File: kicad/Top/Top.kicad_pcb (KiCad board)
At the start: 4 copper layers, 143.5 x 101.6 mm, 295 parts, among them J1 ED120/2DS, J10 Header 2x3, J13 Header 2x5, J14 PACK CONNECT, J15 CELL CONNECT, J2 ED120/2DS, J3 ED120/2DS, J4 USBC_Receptacle_SMD_RA, J5 ED120/4DS, J6 M20-9990246, J8 0022053041, J9 N2510-6002-RB, Q1 CSD17581Q3A, Q2 CSD17581Q3A, Q3 CSD17581Q3A, Q4 CSD17581Q3A, Q5 CSD17575Q3, Q6 SI4477DY-T1-GE3, Q7 SI4477DY-T1-GE3, Q8 PMBF170,235, Q9 PMBF170,235, U1 BQ25790YBG, U2 TLV76033DBZR, U3 MCP1804 SOT-23-5, U4 UPD301C QFN-40, U5 EFC8811R-TF, U6 BQ2980RUG

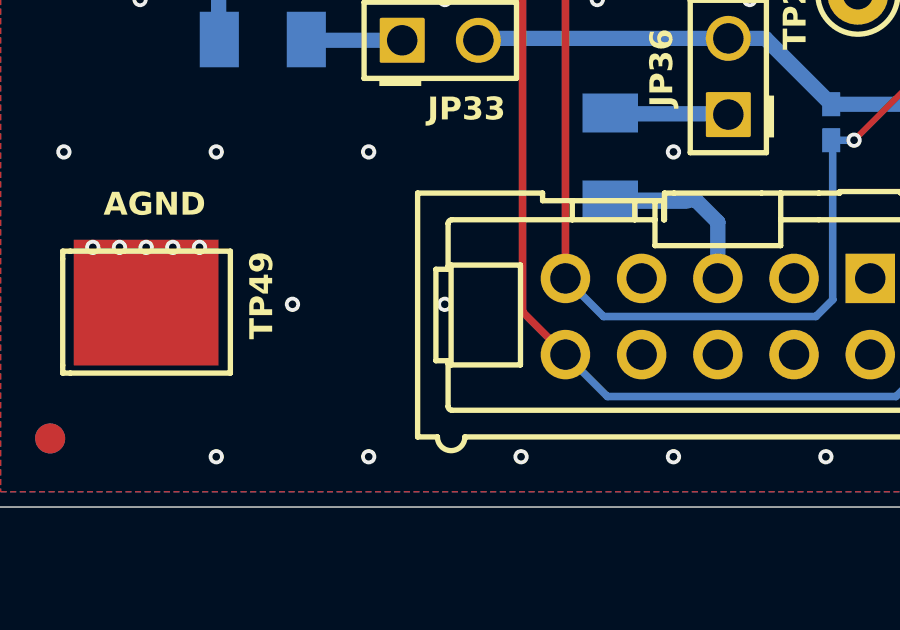
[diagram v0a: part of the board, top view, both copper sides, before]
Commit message: Properly synced pcb to schematic
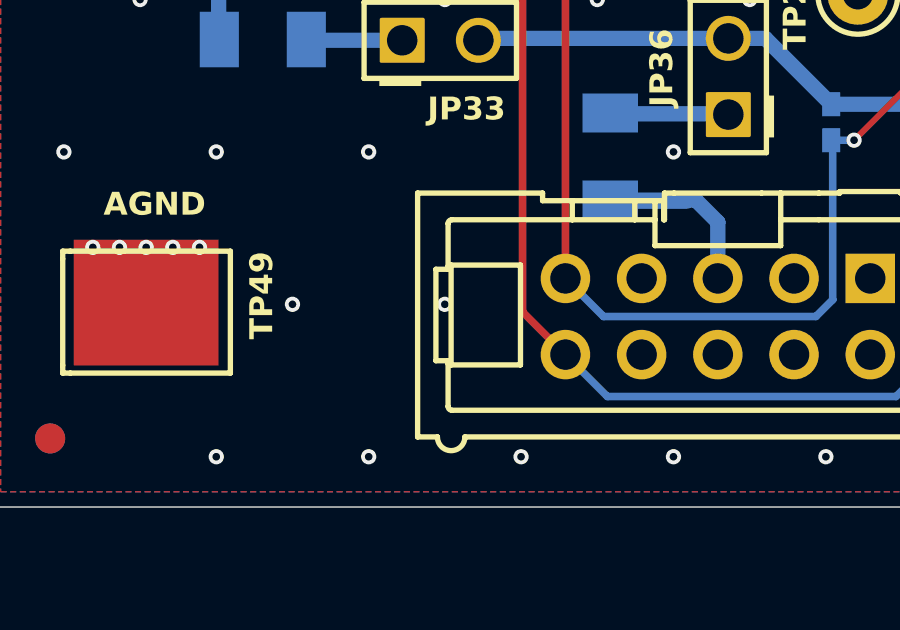
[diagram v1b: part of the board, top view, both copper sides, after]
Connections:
- net /CE renamed /CE
- net /INT renamed /INT
- net /PG renamed /PG
- net /QON renamed /QON
- net 1.5A_IND renamed /Designator/Designator/1.5A_IND
- net 3.0A_IND renamed /Designator/Designator/3.0A_IND
- net BAT_PRO renamed /Designator/BAT_PRO
- net BAT_Physical renamed /Designator/BAT_Physical
- net BTST1 renamed /Designator/U_Charger_Circuit/BTST1
- net BTST2 renamed /Designator/U_Charger_Circuit/BTST2
- net CAP_MISMATCH renamed /Designator/Designator/CAP_MISMATCH
- net CC1 renamed /Designator/Designator/CC1
- net CC1_R renamed /Designator/Designator/CC1_R
- net CC2 renamed /Designator/Designator/CC2
- net CC2_R renamed /Designator/Designator/CC2_R
- net CS renamed /Designator/CS
- net CTR renamed /Designator/CTR
- net D+_1 renamed /Designator/U_Charger_Circuit/D+_1
- net D-_1 renamed /Designator/U_Charger_Circuit/D-_1
- net DAC_I renamed /Designator/Designator/DAC_I
- net EN_SNK renamed /Designator/Designator/EN_SNK
- net FAULT_IN_N renamed /Designator/Designator/FAULT_IN_N
- net IBAT renamed /Designator/U_Charger_Circuit/IBAT
- net NetC12_1 renamed Net-(C12-Pad1)
- net NetC18_2 renamed Net-(C18-Pad2)
- net NetC2_1 renamed Net-(C2-Pad1)
- net NetC2_2 renamed Net-(C2-Pad2)
- net NetC39_2 renamed Net-(C39-Pad2)
- net NetC40_1 renamed Net-(C40-Pad1)
- net NetC42_2 renamed Net-(C42-Pad2)
- net NetC5_1 renamed Net-(C5-Pad1)
- net NetC5_2 renamed Net-(C5-Pad2)
- net NetC6_1 renamed Net-(C6-Pad1)
- net NetD10_1 renamed Net-(D10-Pad1)
- net NetD11_1 renamed Net-(D11-Pad1)
- net NetD13_1 renamed Net-(D13-Pad1)
- net NetD13_2 renamed Net-(D13-Pad2)
- net NetD14_1 renamed Net-(D14-Pad1)
- net NetD14_2 renamed Net-(D14-Pad2)
- net NetD15_1 renamed Net-(D15-Pad1)
- net NetD17_1 renamed Net-(D17-Pad1)
- net NetD18_1 renamed Net-(D18-Pad1)
- net NetJ10_1 renamed I2C_SLAVE_IRQ
- net NetJ10_2 renamed DEBUG_TRACE_TX
- net NetJ10_3 renamed I2C_SLAVE_SDA
- net NetJ10_4 renamed DEBUG_TRACE_RX
- net NetJ10_5 renamed I2C_SLAVE_SCL
- net NetJ13_2 renamed TRGT_SWDIO
- net NetJ13_4 renamed TRGT_SWCLK
- net NetJ3_1 renamed Net-(J3-Pad1)
- net NetJ8_4 renamed Net-(J8-Pad4)
- net NetJ9_5 renamed Net-(J9-Pad5)
- net NetJP14_2 renamed Net-(JP14-Pad2)
- net NetJP15_2 renamed Net-(JP15-Pad2)
- net NetJP16_2 renamed Net-(JP16-Pad2)
- net NetJP24_2 renamed Net-(JP24-Pad2)
- net NetJP25_2 renamed Net-(JP25-Pad2)
- net NetJP32_2 renamed Net-(JP32-Pad2)
- net NetJP33_1 renamed Net-(JP33-Pad1)
- net NetJP36_1 renamed Net-(JP36-Pad1)
- net NetJP5_1 renamed Net-(JP5-Pad1)
- net NetQ6_4 renamed Net-(Q6-Pad4)
- net NetQ8_3 renamed Net-(Q8-Pad3)
- net NetQ9_3 renamed Net-(Q9-Pad3)
- net NetR38_1 renamed Net-(R38-Pad1)
- net NetR47_2 renamed Net-(R47-Pad2)
- net NetR56_1 renamed PDO_SEL
- net NetR59_1 renamed Net-(R59-Pad1)
- net NetR60_1 renamed Net-(R60-Pad1)
- net NetR64_1 renamed Net-(R64-Pad1)
- net ORIENTATION renamed /Designator/Designator/ORIENTATION
- net PACK renamed /Designator/PACK
- net PMID renamed /Designator/U_Charger_Circuit/PMID
- net SDRV renamed /Designator/U_Charger_Circuit/SDRV
- net SPI_MOSI renamed /Designator/Designator/SPI_MOSI
- net SPI_MOSI_SI renamed /Designator/Designator/SPI_MOSI_SI
- net SW1 renamed /Designator/U_Charger_Circuit/SW1
- net SW2 renamed /Designator/U_Charger_Circuit/SW2
- net VBUS_DIS renamed /Designator/Designator/VBUS_DIS
- net VBUS_F renamed /Designator/Designator/VBUS_F
- net VDD renamed /Designator/VDD
- C1 pad 1: VBUS_USB_OUT -> VIN1
- C33 pad 2: NetC33_2 -> unconnected-(C33-Pad2)
- D16 pad 3: NetC33_2 -> unconnected-(C33-Pad2)
- J1 pad 2: VBUS_USB_OUT -> VIN1
- J13 pad 6: (no net) -> unconnected-(J13-Pad6)
- J13 pad 7: (no net) -> unconnected-(J13-Pad7)
- J13 pad 8: (no net) -> unconnected-(J13-Pad8)
- J14 pad 2: BAT_Protection -> /Designator/BAT_Protection
- J4 pad A10: (no net) -> unconnected-(J4-PadA10)
- J4 pad A11: (no net) -> unconnected-(J4-PadA11)
- J4 pad A2: (no net) -> unconnected-(J4-PadA2)
- J4 pad A3: (no net) -> unconnected-(J4-PadA3)
- J4 pad A8: (no net) -> unconnected-(J4-PadA8)
- J4 pad B10: (no net) -> unconnected-(J4-PadB10)
- J4 pad B11: (no net) -> unconnected-(J4-PadB11)
- J4 pad B2: (no net) -> unconnected-(J4-PadB2)
- J4 pad B3: (no net) -> unconnected-(J4-PadB3)
- J4 pad B8: (no net) -> unconnected-(J4-PadB8)
- J5 pad 4: BAT_Protection -> VBAT
- J9 pad 1: (no net) -> unconnected-(J9-Pad1)
- J9 pad 2: (no net) -> unconnected-(J9-Pad2)
- J9 pad 3: (no net) -> unconnected-(J9-Pad3)
- J9 pad 4: (no net) -> unconnected-(J9-Pad4)
- J9 pad 7: (no net) -> unconnected-(J9-Pad7)
- J9 pad 8: (no net) -> unconnected-(J9-Pad8)
- R13 pad 1: BAT_Protection -> VBAT
- R2 pad 1: VBUS_USB_OUT -> VIN1
- R28 pad 1: NetR28_1 -> unconnected-(R28-Pad1)
- R33 pad 1: NetC33_2 -> unconnected-(C33-Pad2)
- R48 pad 2: NetC33_2 -> unconnected-(C33-Pad2)
- R60 pad 2: BAT_Protection -> /Designator/BAT_Protection
- R63 pad 2: BAT_Protection -> /Designator/BAT_Protection
- TP1 pad 1: VBUS_USB_OUT -> VIN1
- TP18 pad 1: BAT_Protection -> VBAT
- U3 pad 3: (no net) -> unconnected-(U3-Pad3)
- U3 pad 4: NetR28_1 -> unconnected-(R28-Pad1)
- U4 pad 1: (no net) -> unconnected-(U4-Pad1)
- U4 pad 13: (no net) -> unconnected-(U4-Pad13)
- U4 pad 22: (no net) -> unconnected-(U4-Pad22)
- U4 pad 23: (no net) -> unconnected-(U4-Pad23)
- U4 pad 24: (no net) -> unconnected-(U4-Pad24)
- U4 pad 27: (no net) -> unconnected-(U4-Pad27)
- U4 pad 29: (no net) -> unconnected-(U4-Pad29)
- U4 pad 3: (no net) -> unconnected-(U4-Pad3)
- U4 pad 9: NetC33_2 -> unconnected-(C33-Pad2)
- U5 pad 1: BAT_Protection -> /Designator/BAT_Protection
- U5 pad 3: BAT_Protection -> /Designator/BAT_Protection
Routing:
- net ACDRV2: track 122.8 -> 0.00 mm, vias 2 -> 0
- net ACDRV1: track 112.3 -> 235.1 mm, vias 0 -> 2
- net BAT_Protection: track 18.9 -> 0.00 mm, vias 15 -> 0
- net unconnected-(C33-Pad2): track 0.00 -> 16.3 mm, vias 0 -> 2
- net NetC33_2: track 16.3 -> 0.00 mm, vias 2 -> 0
- net PGND: track 97.3 -> 110.6 mm, vias 281 -> 282
- net VIN1: track 0.00 -> 12.1 mm
- net VBUS_USB_OUT: track 12.1 -> 0.00 mm
- net VBAT: track 0.00 -> 12.1 mm
- net AGND: track 33.0 -> 22.0 mm
- net /Designator/BAT_Protection: track 0.00 -> 6.79 mm, vias 0 -> 15
- net unconnected-(R28-Pad1): track 0.00 -> 4.38 mm
- net NetR28_1: track 4.38 -> 0.00 mm
- net (no net): track 17.0 -> 14.8 mm, vias 78 -> 77
- added copper zone on F.Cu, net /Designator/BAT_Protection
- removed copper zone on F.Cu, net BAT_Protection

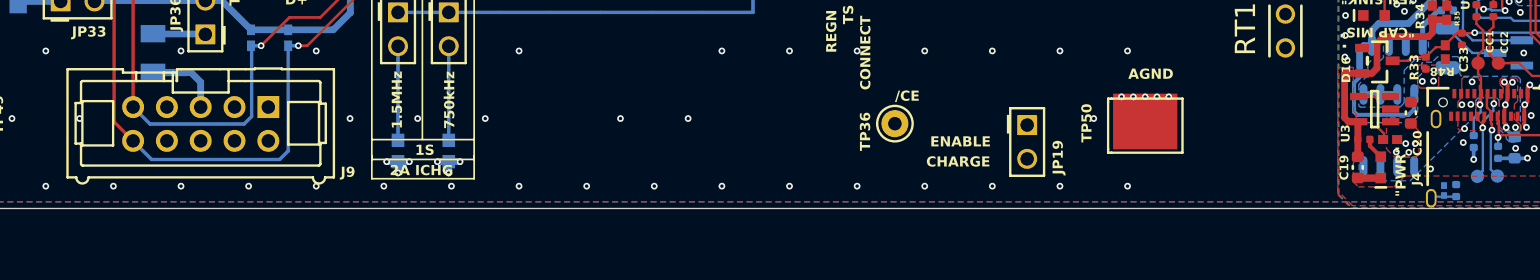
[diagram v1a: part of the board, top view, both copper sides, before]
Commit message: Removed earth net
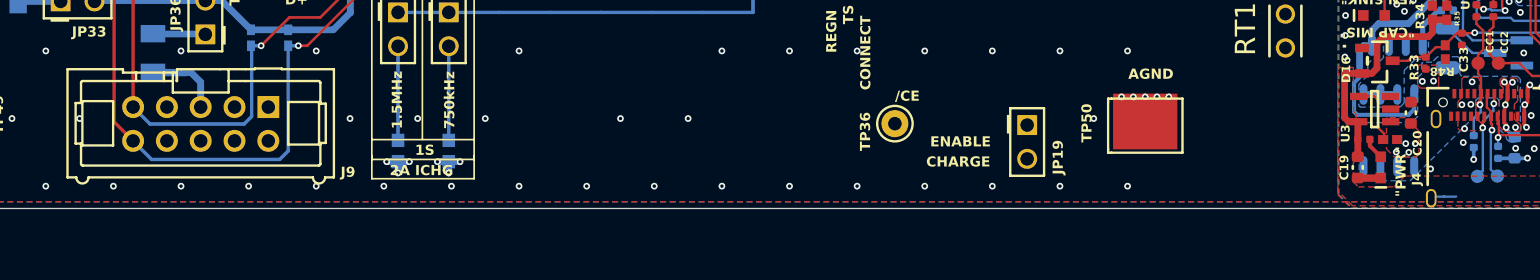
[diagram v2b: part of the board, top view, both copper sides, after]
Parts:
- removed C44: CAP1337, AltiumImports:_ALTIUM_WORK_00001_MCHP-CDB_Library_Database_.._Footprints_CAP_C_0402.PcbLib_CAP_C_0402
- removed R36: CMP-2002-07613-1, AltiumImports:RESC1005X40X25LL05T10
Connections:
- J4 pad 25: EARTH_P1 -> PGND
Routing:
- net PGND: track 110.6 -> 112.5 mm
- net EARTH_P1: track 1.93 -> 0.00 mm

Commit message: Renamed sheets
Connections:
- net /Designator/BAT_PRO renamed /Protection/BAT_PRO
- net /Designator/BAT_Physical renamed /Protection/BAT_Physical
- net /Designator/BAT_Protection renamed /Protection/BAT_Protection
- net /Designator/CS renamed /Protection/CS
- net /Designator/CTR renamed /Protection/CTR
- net /Designator/Designator/1.5A_IND renamed /USB-PD/USB-PD_Circuit/1.5A_IND
- net /Designator/Designator/3.0A_IND renamed /USB-PD/USB-PD_Circuit/3.0A_IND
- net /Designator/Designator/CAP_MISMATCH renamed /USB-PD/USB-PD_Circuit/CAP_MISMATCH
- net /Designator/Designator/CC1 renamed /USB-PD/USB-PD_Circuit/CC1
- net /Designator/Designator/CC1_R renamed /USB-PD/USB-PD_Circuit/CC1_R
- net /Designator/Designator/CC2 renamed /USB-PD/USB-PD_Circuit/CC2
- net /Designator/Designator/CC2_R renamed /USB-PD/USB-PD_Circuit/CC2_R
- net /Designator/Designator/DAC_I renamed /USB-PD/USB-PD_Circuit/DAC_I
- net /Designator/Designator/EN_SNK renamed /USB-PD/USB-PD_Circuit/EN_SNK
- net /Designator/Designator/FAULT_IN_N renamed /USB-PD/USB-PD_Circuit/FAULT_IN_N
- net /Designator/Designator/ORIENTATION renamed /USB-PD/USB-PD_Circuit/ORIENTATION
- net /Designator/Designator/SPI_MOSI renamed /USB-PD/USB-PD_Circuit/SPI_MOSI
- net /Designator/Designator/SPI_MOSI_SI renamed /USB-PD/USB-PD_Circuit/SPI_MOSI_SI
- net /Designator/Designator/VBUS_DIS renamed /USB-PD/USB-PD_Circuit/VBUS_DIS
- net /Designator/Designator/VBUS_F renamed /USB-PD/USB-PD_Circuit/VBUS_F
- net /Designator/PACK renamed /Protection/PACK
- net /Designator/U_Charger_Circuit/BTST1 renamed /Charger/Charger_Circuit/BTST1
- net /Designator/U_Charger_Circuit/BTST2 renamed /Charger/Charger_Circuit/BTST2
- net /Designator/U_Charger_Circuit/D+_1 renamed /Charger/Charger_Circuit/D+_1
- net /Designator/U_Charger_Circuit/D-_1 renamed /Charger/Charger_Circuit/D-_1
- net /Designator/U_Charger_Circuit/IBAT renamed /Charger/Charger_Circuit/IBAT
- net /Designator/U_Charger_Circuit/PMID renamed /Charger/Charger_Circuit/PMID
- net /Designator/U_Charger_Circuit/SDRV renamed /Charger/Charger_Circuit/SDRV
- net /Designator/U_Charger_Circuit/SW1 renamed /Charger/Charger_Circuit/SW1
- net /Designator/U_Charger_Circuit/SW2 renamed /Charger/Charger_Circuit/SW2
- net /Designator/VDD renamed /Protection/VDD
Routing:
- net ACDRV2: track 0.00 -> 122.8 mm, vias 0 -> 2
- net ACDRV1: track 235.1 -> 112.3 mm, vias 2 -> 0
- net AGND: track 22.0 -> 33.0 mm, vias 40 -> 41
- net PGND: track 112.5 -> 101.5 mm, vias 282 -> 281

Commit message: Cleared pcb
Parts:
- removed C1, C4: CMP-0008217-2, AltiumImports:0805L
- removed C10, C21, C22, C23, C27, C28, C29, C30, C31, C7, C8, C9: C2012X5R1E106K125AB, AltiumImports:0805_HV
- removed C11, C14, C15, C24, C26: C1005X7R1H104K050BE, AltiumImports:0402L
- removed C12, C6: GRM1885C1H222JA01D, AltiumImports:0603
- removed C13, C3: GRM155R71E473KA88D, AltiumImports:0402
- removed C16, C17: C0402C103J5RACTU, AltiumImports:0402
- removed C18, C46: Capacitor NP, AltiumImports:_ALTIUM_WORK_00001_MCHP-CDB_Library_Database_MCHP-CDB.DbLib_Capacitor_CAP_C_0603
- removed C19, C20: Capacitor NP, AltiumImports:_ALTIUM_WORK_00001_MCHP-CDB_Library_Database_.._Footprints_CAP_C_0603.PcbLib_CAP_C_0603
- removed C2, C39, C5: GRM1555C1H102FA01D, AltiumImports:0402
- removed C25, C32, C47, C48: Capacitor NP, AltiumImports:_ALTIUM_WORK_00001_MCHP-CDB_Library_Database_MCHP-CDB.DbLib_Capacitor_CAP_C_0402
- removed C33, C45, C53: CAP1337, AltiumImports:_ALTIUM_WORK_00001_MCHP-CDB_Library_Database_.._Footprints_CAP_C_0402.PcbLib_CAP_C_0402
- removed C34: GRM188R61C475KAAJD, AltiumImports:0603L
- removed C35, C42, C43: GRM155R61E104KA87D, AltiumImports:0402L
- removed C36, C37, C38: GRT188R61E106ME13D, AltiumImports:0603L
- removed C40, C41: GRM1555C1H102JA01D, AltiumImports:0402L
- removed C49, C51, C52: CAP1337, AltiumImports:CAP_C_0402
- removed C50: Capacitor NP, AltiumImports:CAP_C_0603
- removed C54, C55, C56: GRM188R71H104KA93D, AltiumImports:0603L
- removed D1, D10, D4: CMP-0028378-3, AltiumImports:SOD-523
- removed D11, D12: BAT54HT1G, AltiumImports:SOD-323
- removed D13, D14: LTST-C190GKT, AltiumImports:LED_LTST-C190
- removed D15, D17: LED_green, AltiumImports:_ALTIUM_WORK_00001_MCHP-CDB_Library_Database_.._Footprints_LED_0603_Green.PcbLib_LED_0603_GREEN
- removed D16: Diode Dual AK, AltiumImports:SOT-23-3
- removed D18: LED_orange, AltiumImports:_ALTIUM_WORK_00001_MCHP-CDB_Library_Database_.._Footprints_LED_0603_Orange.PcbLib_LED_0603_Orange
- removed D2, D5, D9: BZT52C12T-7, AltiumImports:SOD-523
- removed D3, D6, D7, D8: B130LAW-7-F, AltiumImports:SOD-123
- removed FB1: Ferrite Bead, AltiumImports:IND_C_0603
- removed FID1, FID2, FID3, FID4, FID5, FID6: CMP-0077181-1, AltiumImports:Fiducial10-20
- removed H1, H2, H3, H4: SJ-5303 (CLEAR), AltiumImports:Bumpon_SJ5003Transparent
- removed J1, J2, J3: ED120/2DS, AltiumImports:On-Shore_ED120_2DS
- removed J10: Header 2x3, AltiumImports:_ALTIUM_WORK_00001_MCHP-CDB_Library_Database_MCHP-CDB.DbLib_Connector_HDR_M_2.54_2x3
- removed J13: Header 2x5, AltiumImports:_ALTIUM_WORK_00001_MCHP-CDB_Library_Database_MCHP-CDB.DbLib_Connector_HDR_M_1.27_2x5_TH_V_FCI_20021111-00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
- removed J14: PACK CONNECT, AltiumImports:TERM_BLK_ED555-2DS
- removed J15: CELL CONNECT, AltiumImports:TERM_BLK_ED555-2DS
- removed J4: USBC_Receptacle_SMD_RA, AltiumImports:CON_USB3.1-C_RCPT_SMD_RA_ACP_12401610E4#2A
- removed J5: ED120/4DS, AltiumImports:On-Shore_ED120_4DS
- removed J6: M20-9990246, AltiumImports:FP-M20-9990246-MFG
- removed J8: 0022053041, AltiumImports:CONN_22-05-3041
- removed J9: N2510-6002-RB, AltiumImports:CONN_2510-6002
- removed JP1, JP11, JP2: PEC03SAAN, AltiumImports:CONN_PEC03SAAN
- removed JP10, JP19, JP32, JP33, JP34, JP35, JP36, JP6: Header_2x1, AltiumImports:CONN_PEC02SAAN
- removed JP12, JP13, JP14, JP15, JP16, JP23, JP24, JP25, JP9: CMP-0002337-1, AltiumImports:CONN_PEC02SAAN
- removed JP3, JP4, JP5: HTSW-102-07-G-S, AltiumImports:Samtec_HTSW-102-07-G-S
- removed L1: MPIM252010F1R0M-LF, AltiumImports:MPIM252010F
- removed L2: SPM6530T-2R2M, AltiumImports:SPM6530
- removed LOGO5: CAUTION HOT SURFACE, AltiumImports:IEC_HotSurface_Small
- removed NT1: CMP-0078142-3, AltiumImports:Net-Tie_20milWide_60milLong
- removed Q1, Q2, Q3, Q4: CSD17581Q3A, AltiumImports:DNH0008A
- removed Q5: CSD17575Q3, AltiumImports:DQG0008A
- removed Q6, Q7: SI4477DY-T1-GE3, AltiumImports:_ALTIUM_WORK_00001_MCHP-CDB_Library_Database_.._Footprints_SOIC-8.PcbLib_SOIC-8
- removed Q8, Q9: PMBF170,235, AltiumImports:NXP-SOT23_M
- removed R1, R14, R38, R5: 5106, AltiumImports:5106
- removed R10, R8: CRCW06032R00JNEA, AltiumImports:0603
- removed R11: Resistor, AltiumImports:RES_C_1206
- removed R12, R13, R2, R6: WSL2010R0100FEA18, AltiumImports:2010
- removed R15, R3, R7: RC0402FR-07100KL, AltiumImports:0402
- removed R16: CMP-0025697-4, AltiumImports:0603L
- removed R17, R18: RC0603FR-07100RL, AltiumImports:0603
- removed R19: CMP-0026464-2, AltiumImports:0402
- removed R20, R42, R43, R44, R45: CRCW040210K0FKED, AltiumImports:0402
- removed R21: 47k, AltiumImports:FP-CRCW0603-e3-IPC_B
- removed R22: CRCW0603255KFKEA, AltiumImports:0603
- removed R23, R24, R27, R33, R50, R52, R56: Resistor, AltiumImports:_ALTIUM_WORK_00001_MCHP-CDB_Library_Database_MCHP-CDB.DbLib_Resistor_RES_C_0402
- removed R25: RC0603FR-07100KL, AltiumImports:0603
- removed R26: CMP-0026284-2, AltiumImports:0402
- removed R28, R34, R35, R48, R54, R55: CRGP0402F10K, AltiumImports:FP-CRGP0402-IPC_A
- removed R29: RC0603FR-073KL, AltiumImports:0603
- removed R30: RC0603FR-074K7L, AltiumImports:0603
- removed R31, R49: Resistor, AltiumImports:_ALTIUM_WORK_00001_MCHP-CDB_Library_Database_MCHP-CDB-Offline.DbLib_Resistor_RES_C_0402
- removed R32, R47, R51, R53, R57, R58: Resistor, AltiumImports:_ALTIUM_WORK_00001_MCHP-CDB_Library_Database_.._Footprints_RES_C_0402.PcbLib_RES_C_0402
- removed R37, R39, R46: ERJ-8ENF10R0V, AltiumImports:1206
- removed R4, R9: CRCW0603294RFKEA, AltiumImports:0603
- removed R40, R41: CRCW04022K21FKED, AltiumImports:0402
- removed R59, R60: CRCW04025M10JNED, AltiumImports:0402L
- removed R61: CRCW0402330RJNED, AltiumImports:0402L
- removed R62: CRCW040220R0FKED, AltiumImports:0402L
- removed R63: CRCW04022K00FKED, AltiumImports:0402L
- removed R64: CRCW0402100RFKED, AltiumImports:0402L
- removed R65: R_SEN, AltiumImports:1206
- removed RT1: 103AT-2, AltiumImports:SEMI-103AT-2_V
- removed S1: CMP-0002170-2, AltiumImports:KSR
- removed SH-JP1: ACDRV1 to _acdrv1, AltiumImports:FP-SNT-100-BK-G-MFG
- removed SH-JP10, SH-JP11, SH-JP12, SH-JP14, SH-JP16, SH-JP19, SH-JP32, SH-JP34, SH-JP35, SH-JP36, SH-JP37, SH-JP6, SH-JP9: Installed, AltiumImports:FP-SNT-100-BK-G-MFG
- removed SH-JP13, SH-JP15, SH-JP23, SH-JP24, SH-JP25, SH-JP3, SH-JP33, SH-JP4, SH-JP5: Not Installed, AltiumImports:FP-SNT-100-BK-G-MFG
- removed SH-JP2: ACDRV2 to _acdrv2, AltiumImports:FP-SNT-100-BK-G-MFG
- removed TP1, TP10, TP11, TP12, TP15, TP16, TP17, TP18, TP19, TP2, TP20, TP28, TP29, TP3, TP30, TP31, TP32, TP33, TP34, TP35, TP36, TP37, TP38, TP39, TP4, TP40, TP41, TP42, TP43, TP44, TP5, TP6, TP7, TP8, TP9: CMP-0055139-1, AltiumImports:Keystone5002
- removed TP13, TP14, TP52, TP53, TP54, TP55, TP56, TP57, TP58, TP59: Test Point No BOM, AltiumImports:_ALTIUM_WORK_00001_MCHP-CDB_Library_Database_.._Footprints_TP_1mm_SMD.PcbLib_TP_1mm_SMD
- removed TP21, TP22, TP23, TP24: CMP-0055137-1, AltiumImports:Keystone5000
- removed TP25, TP26: CMP-0055140-1, AltiumImports:Keystone5003
- removed TP27: CMP-0055141-1, AltiumImports:Keystone5004
- removed TP45, TP46, TP47, TP48, TP49, TP50, TP51: CMP-0055153-1, AltiumImports:Testpoint_Keystone_Compact
- removed TP60: G_CHG, AltiumImports:TESTPOINT
- removed TP61: G_DSG, AltiumImports:TESTPOINT
- removed TP62: CTR, AltiumImports:Keystone5012
- removed U1: BQ25790YBG, AltiumImports:PREYBG0056
- removed U2: TLV76033DBZR, AltiumImports:DBZ0003A_N
- removed U3: MCP1804 SOT-23-5, AltiumImports:_ALTIUM_WORK_00001_MCHP-CDB_Library_Database_MCHP-CDB.DbLib_MCHP-Analog_SOT-23-5
- removed U4: UPD301C QFN-40, AltiumImports:_ALTIUM_WORK_00001_MCHP-CDB_Library_Database_MCHP-CDB.DbLib_MCHP-Interface_QFN-40_6X6_m5_4m6epad
- removed U5: EFC8811R-TF, AltiumImports:CSP6_568AL
- removed U6: BQ2980RUG, AltiumImports:RUG0008A
- moved ZZ1 26.5 mm to (59.6, 16.6)
- moved ZZ2 26.5 mm to (59.6, 22.9)
- moved ZZ3 26.5 mm to (59.6, 29.3)
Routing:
- net REGN: track 195.8 -> 0.00 mm, vias 3 -> 0
- net VBUS: track 156.0 -> 0.00 mm, vias 52 -> 0
- net BAT_U1: track 138.0 -> 0.00 mm, vias 25 -> 0
- net ACDRV2: track 122.8 -> 0.00 mm, vias 2 -> 0
- net VAC2: track 121.2 -> 0.00 mm, vias 19 -> 0
- net /Charger/Charger_Circuit/SDRV: track 113.3 -> 0.00 mm, vias 2 -> 0
- net ACDRV1: track 112.3 -> 0.00 mm
- net SYS: track 111.0 -> 0.00 mm, vias 34 -> 0
- net VAC1: track 110.8 -> 0.00 mm, vias 21 -> 0
- net SDA: track 106.3 -> 0.00 mm, vias 1 -> 0
- net SCL: track 104.6 -> 0.00 mm, vias 1 -> 0
- net PGND: track 101.5 -> 0.00 mm, vias 281 -> 0
- net ILIM_HIZ: track 98.6 -> 0.00 mm, vias 2 -> 0
- net /Charger/Charger_Circuit/PMID: track 98.3 -> 0.00 mm, vias 4 -> 0
- net /Charger/Charger_Circuit/BTST2: track 85.0 -> 0.00 mm, vias 1 -> 0
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- removed copper zone on B.Cu, net (none)
- removed copper zone on F.Cu, net (none)
- removed copper zone on F.Cu, net /Charger/Charger_Circuit/PMID
- removed copper zone on F.Cu, net /Charger/Charger_Circuit/SW1
- removed copper zone on In2.Cu, net /Charger/Charger_Circuit/SW1
- removed copper zone on F.Cu, net /Charger/Charger_Circuit/SW2
- removed copper zone on In2.Cu, net /Charger/Charger_Circuit/SW2
- removed copper zone on F.Cu, net /Protection/BAT_PRO
- removed copper zone on F.Cu, net /Protection/BAT_Physical
- removed copper zone on F.Cu, net /Protection/BAT_Protection
- removed copper zone on F.Cu, net /Protection/CS
- removed copper zone on B.Cu, net /USB-PD/USB-PD_Circuit/VBUS_F
- removed copper zone on B.Cu, net 3V3_U3
- removed copper zone on F.Cu, net 3V3_U3
- removed copper zone on In2.Cu, net AGND
- removed copper zone on B.Cu, net BAT_U1
- removed copper zone on F.Cu, net BAT_U1
- removed copper zone on F.Cu, net Net-(C2-Pad1)
- removed copper zone on F.Cu, net Net-(C5-Pad1)
- removed copper zone on F.Cu, net Net-(JP5-Pad1)
- removed copper zone on B.Cu, net PGND
- removed copper zone on F.Cu, net PGND
- removed copper zone on In1.Cu, net PGND
- removed copper zone on F.Cu, net SYS
- removed copper zone on F.Cu, net VAC1
- removed copper zone on F.Cu, net VAC2
- removed copper zone on B.Cu, net VBUS
- removed copper zone on F.Cu, net VBUS
- removed copper zone on B.Cu, net VBUS_USB
- removed copper zone on B.Cu, net VDD33
- removed copper zone on F.Cu, net VDD33
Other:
- board outline removed
- board text removed: ""CAP MIS""
- board text removed: ""EN SINK""
- board text removed: ""PWR""
- board text removed: "${LAYER}"
- board text removed: "'.Layer_Name'"
- board text removed: "'.PRJ_Number' '.PCB_Rev'"
- board text removed: "(+)"
- board text removed: "(-)"
- board text removed: "(Mixed)"
- board text removed: "+/-"
- board text removed: "."
- board text removed: ".Application_BuildNumber"
- board text removed: ".PCB_File_Name_No_Path"
- board text removed: ".PCB_Rev"
- board text removed: ".PRJ_Customer"
- board text removed: ".PRJ_Engineer"
- board text removed: ".PRJ_Number"
- board text removed: ".PRJ_Title"
- board text removed: ".Print_Date"
- board text removed: ".Print_Time"
- board text removed: ".TID"
- board text removed: ".VariantName"
- board text removed: ".VersionControl_RevNumber"
- board text removed: ".plot_File_Name"
- board text removed: ".print_Scale"
- board text removed: "/CE"
- board text removed: "/INT"
- board text removed: "/PG"
- board text removed: "/QON"
- board text removed: "0.05mm (2MIL)"
- board text removed: "0.40mil"
- board text removed: "1"
- board text removed: "1.40mil"
- board text removed: "1.5A"
- board text removed: "1.5A_IND"
- board text removed: "1.5MHz"
- board text removed: "10"
- board text removed: "10.00mil (0.254mm)"
- board text removed: "101"
- board text removed: "12.00mil"
- board text removed: "12.00mil (0.305mm)"
- board text removed: "134"
- board text removed: "14.00mil (0.356mm)"
- board text removed: "19.69mil (0.500mm)"
- board text removed: "1MIL"
- board text removed: "1S"
- board text removed: "2"
- board text removed: "25.59mil (0.650mm)"
- board text removed: "28.00mil (0.711mm)"
- board text removed: "2A ICHG"
- board text removed: "3"
- board text removed: "3.00mil (0.076mm)"
- board text removed: "3.0A IND"
- board text removed: "3.5"
- board text removed: "31 MIL +/-10%"
- board text removed: "31.00mil"
- board text removed: "35"
- board text removed: "35.43mil (0.900mm)"
- board text removed: "37.40mil (0.950mm)"
- board text removed: "37.99mil (0.965mm)"
- board text removed: "4"
- board text removed: "4.2"
- board text removed: "40.00mil (1.016mm)"
- board text removed: "40.16mil (1.020mm)"
- board text removed: "49.21mil (1.250mm)"
- board text removed: "5"
- board text removed: "5.7"
- board text removed: "50.00mil (1.270mm)"
- board text removed: "500mA"
- board text removed: "512"
- board text removed: "57"
- board text removed: "5A MAX"
- board text removed: "6"
- board text removed: "6.00mil (0.152mm)"
- board text removed: "62 MIL (1.6mm) +/-10%"
- board text removed: "63.00mil (1.600mm)"
- board text removed: "7"
- board text removed: "7.87mil (0.200mm)"
- board text removed: "750kHz"
- board text removed: "8"
- board text removed: "900 Total"
- board text removed: "= Calculated from tool start centre position to tool end centre position."
- board text removed: "= Routed Path Length + Tool Size = Slot length as defined in the PCB layout"
- board text removed: "A"
- board text removed: "ACDRV1"
- board text removed: "ACDRV2"
- board text removed: "ADDITIONAL REQUIREMENTS:"
- board text removed: "AGND"
- board text removed: "ALL ARTWORK VIEWED FROM TOP SIDE"
- board text removed: "ALL BOARDS MUST MEET OR EXCEED UL94-V0 REQUIREMENTS."
- board text removed: "ALTIUM DESIGNER VERSION:"
- board text removed: "ANSI IPC-6012 TYPE 3 CLASS 2"
- board text removed: "ANSI IPC-A-600F CLASS ->"
- board text removed: "ARRAY/PANEL:"
- board text removed: "AS SHOWN"
- board text removed: "ASSEMBLY VARIANT:"
- board text removed: "BARE BOARD ELEC. TEST:"
- board text removed: "BAT"
- board text removed: "BAT +"
- board text removed: "BAT -"
- board text removed: "BAT-BATTERY"
- board text removed: "BATN"
- board text removed: "BATP"
- board text removed: "BATTERY"
- board text removed: "BOARD #:"
- board text removed: "BOARD FINISH:"
- board text removed: "BOTTOM"
- board text removed: "BOW & TWIST:"
- board text removed: "BTST1"
- board text removed: "BTST2"
- board text removed: "BYPASS"
- board text removed: "Board Layer Stack"
- board text removed: "Bottom Layer"
- board text removed: "Bottom Overlay"
- board text removed: "Bottom Solder"
- board text removed: "C"
- board text removed: "CC1"
- board text removed: "CC2"
- board text removed: "CERTIFICATION:"
- board text removed: "CHARGE"
- board text removed: "COMPONENTS MARKED 'DNP' SHOULD NOT BE POPULATED."
- board text removed: "CONNECT"
- board text removed: "CUT AND TRIM PER M1 BOARD OUTLINE"
- board text removed: "Constant"
- board text removed: "Count"
- board text removed: "D"
- board text removed: "D+"
- board text removed: "D-"
- board text removed: "DAC_I"
- board text removed: "DBG I/F"
- board text removed: "DESIGN INFORMATION"
- board text removed: "DESIGNED FOR:"
- board text removed: "DN"
- board text removed: "DP"
- board text removed: "DRILLING:"
- board text removed: "Dielectric 2"
- board text removed: "Dielectric 3"
- board text removed: "Dielectric1"
- board text removed: "Drill Layer Pair"
- board text removed: "EN"
- board text removed: "ENABLE"
- board text removed: "ENEPIG"
- board text removed: "ENGINEER:"
- board text removed: "EXT"
- board text removed: "EXTERNAL"
- board text removed: "FAULT IN"
- board text removed: "FETs"
- board text removed: "FILE NAME:"
- board text removed: "FR-4 High TG"
- board text removed: "FR-4 High Tg"
- board text removed: "FR-408"
- board text removed: "GENERATED :"
- board text removed: "GREEN"
- board text removed: "HIZ"
- board text removed: "HOLE SIZE TOLERANCE (UNLESS OTHERWISE SPECIFIED):"
- board text removed: "Hole Length"
- board text removed: "Hole Size"
- board text removed: "Hole Tolerance (+)"
- board text removed: "Hole Tolerance (-)"
- board text removed: "Hole Type"
- board text removed: "IBAT"
- board text removed: "IINDPM"
- board text removed: "IMM. TIN/SILVER OR EQUIV"
- board text removed: "IMMERSION GOLD (ENIG)"
- board text removed: "IPC-D-275 CLASS 2 LEVEL C"
- board text removed: "I_BAT"
- board text removed: "I_SYS"
- board text removed: "I_VAC1"
- board text removed: "I_VAC2"
- board text removed: "JMM"
- board text removed: "LAYER NAME ="
- board text removed: "LAYOUT BY:"
- board text removed: "LED"
- board text removed: "Layer"
- board text removed: "MATERIAL:"
- board text removed: "MATERIALS AND WORKMANSHIP FOR ALL PCBS"
- board text removed: "MATTE"
- board text removed: "METAL"
- board text removed: "MICROSECTION:"
- board text removed: "MIL"
- board text removed: "MIL, HOLES"
- board text removed: "MIN. CLEARANCE:"
- board text removed: "MIN. TRACK WIDTH:"
- board text removed: "MIN. VIA PAD SIZE:"
- board text removed: "MINIMUM ANNULAR RING"
- board text removed: "Material"
- board text removed: "N.C. ROUTE"
- board text removed: "NC_DRILL FILES"
- board text removed: "NONE"
- board text removed: "NPTH"
- board text removed: "Name"
- board text removed: "ORIENT"
- board text removed: "OTHER"
- board text removed: "OTHER +/-"
- board text removed: "PACK +"
- board text removed: "PACK -"
- board text removed: "PCB MUST BEAR THE UL94V-0 UL REGISTERED MATERIAL ID NUMBER"
- board text removed: "PCB VIEWED FROM BOTTOM SIDE"
- board text removed: "PCB VIEWED FROM TOP SIDE"
- board text removed: "PDO SEL"
- board text removed: "PER"
- board text removed: "PER ORDER"
- board text removed: "PGND"
- board text removed: "PLOT NAME ="
- board text removed: "PMID"
- board text removed: "PROG"
- board text removed: "PROJECT TITLE:"
- board text removed: "PTH"
- board text removed: "PTH MIN COPPER THICKNESS:"
- board text removed: "PULLUP"
- board text removed: "PWR OUT"
- board text removed: "Pad"
- board text removed: "Pad Shape"
- board text removed: "Plated"
- board text removed: "REFERENCE:"
- board text removed: "REGISTRATION TOLERANCES:"
- board text removed: "REGN"
- board text removed: "REQUIRED"
- board text removed: "REV:"
- board text removed: "RoHS"
- board text removed: "Round"
- board text removed: "Rounded"
- board text removed: "Routed Path Length"
- board text removed: "SCL"
- board text removed: "SDA"
- board text removed: "SDRV"
- board text removed: "SEMI-GLOSS"
- board text removed: "SENSE"
- board text removed: "SILKSCREEN COLOR:"
- board text removed: "SILKSCREEN:"
- board text removed: "SOLDER RESIST COLOR:"
- board text removed: "STAT"
- board text removed: "SURFACE FINISH:"
- board text removed: "SVN REV:"
- board text removed: "SW1"
- board text removed: "SW2"
- board text removed: "SYS"
- board text removed: "SYSTEM"
- board text removed: "Signal Layer 1"
- board text removed: "Signal Layer 2"
- board text removed: "Slot"
- board text removed: "Slot definitions :"
- board text removed: "Solder Resist"
- board text removed: "Symbol"
- board text removed: "TEXAS INSTRUMENTS"
- board text removed: "THERM"
- board text removed: "THICKNESS:"
- board text removed: "TID #:"
- board text removed: "TO MEET OR EXCEED THE REQUIREMENTS OF:"
- board text removed: "TOLERANCE:"
- board text removed: "TOP"
- board text removed: "TS"
- board text removed: "Template"
- board text removed: "Texas Instruments (TI) and/or its licensors do not warrant the accuracy or completeness of this specification"
- board text removed: "Thickness"
- board text removed: "Top Layer"
- board text removed: "Top Layer - Bottom Layer"
- board text removed: "Top Overlay"
- board text removed: "Top Solder"
- board text removed: "USB D+"
- board text removed: "USB D-"
- board text removed: "V. SCORE"
- board text removed: "VAC1"
- board text removed: "VAC1-VBUS"
- board text removed: "VAC2"
- board text removed: "VAC2-BUS"
- board text removed: "VBUS"
- board text removed: "VBUS/VBAT"
- board text removed: "VIN1"
- board text removed: "VIN2"
- board text removed: "Via"
- board text removed: "Via Fill:"
- board text removed: "Via/Pad"
- board text removed: "Vias with 10 mil pad / 6 mil drill need to be filled with non-conductive epoxy and plated over."
- board text removed: "WHITE"
- board text removed: "X"
- board text removed: "YES"
- board text removed: "an implementation. TI and/or its licensors do not warrant that the design is production worthy. You should"
- board text removed: "c145h95"
- board text removed: "c203h96"
- board text removed: "c221h160"
- board text removed: "c65hn65p32"
- board text removed: "completely validate and test your design implementation to confirm the system functionality for your application."
- board text removed: "or any information contained therein. TI and/or its licensors do not warrant that this design will meet"
- board text removed: "r140_80h50_110r100m140_80p-1_-1"
- board text removed: "r95_65hn65_95r100p62_32"
- board text removed: "s o l u t i o n s"
- board text removed: "the specifications, will be suitable for your application or fit for any particular purpose, or will operate in"
- board text removed: "v127h71"
- board text removed: "v76h36"
